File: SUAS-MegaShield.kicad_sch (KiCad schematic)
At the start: 1 part

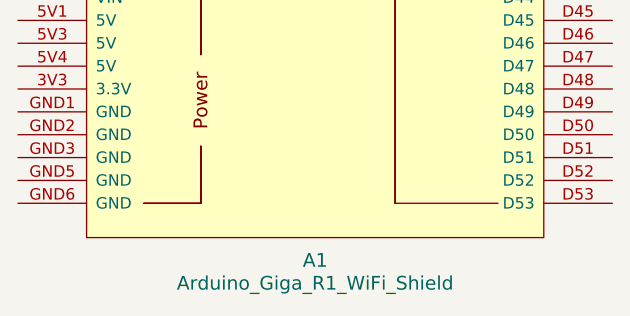
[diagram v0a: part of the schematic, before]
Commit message: Format Changes
- moved Silkscreen from front to back
- added edgeCut
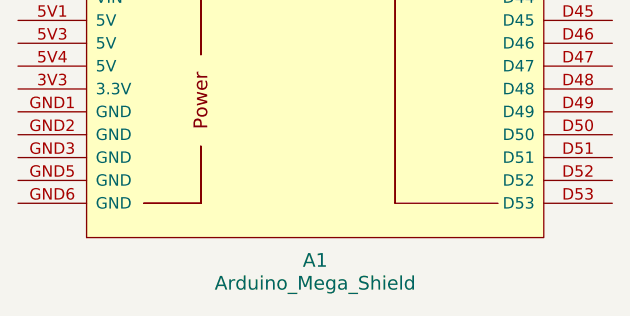
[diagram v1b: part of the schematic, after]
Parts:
- A1: value Arduino_Giga_R1_WiFi_Shield -> Arduino_Mega_Shield
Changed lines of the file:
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@@
 			)
 		)
-		(property "Value" "Arduino_Giga_R1_WiFi_Shield"
+		(property "Value" "Arduino_Mega_Shield"
 			(at 92.71 176.53 0)
 			(effects

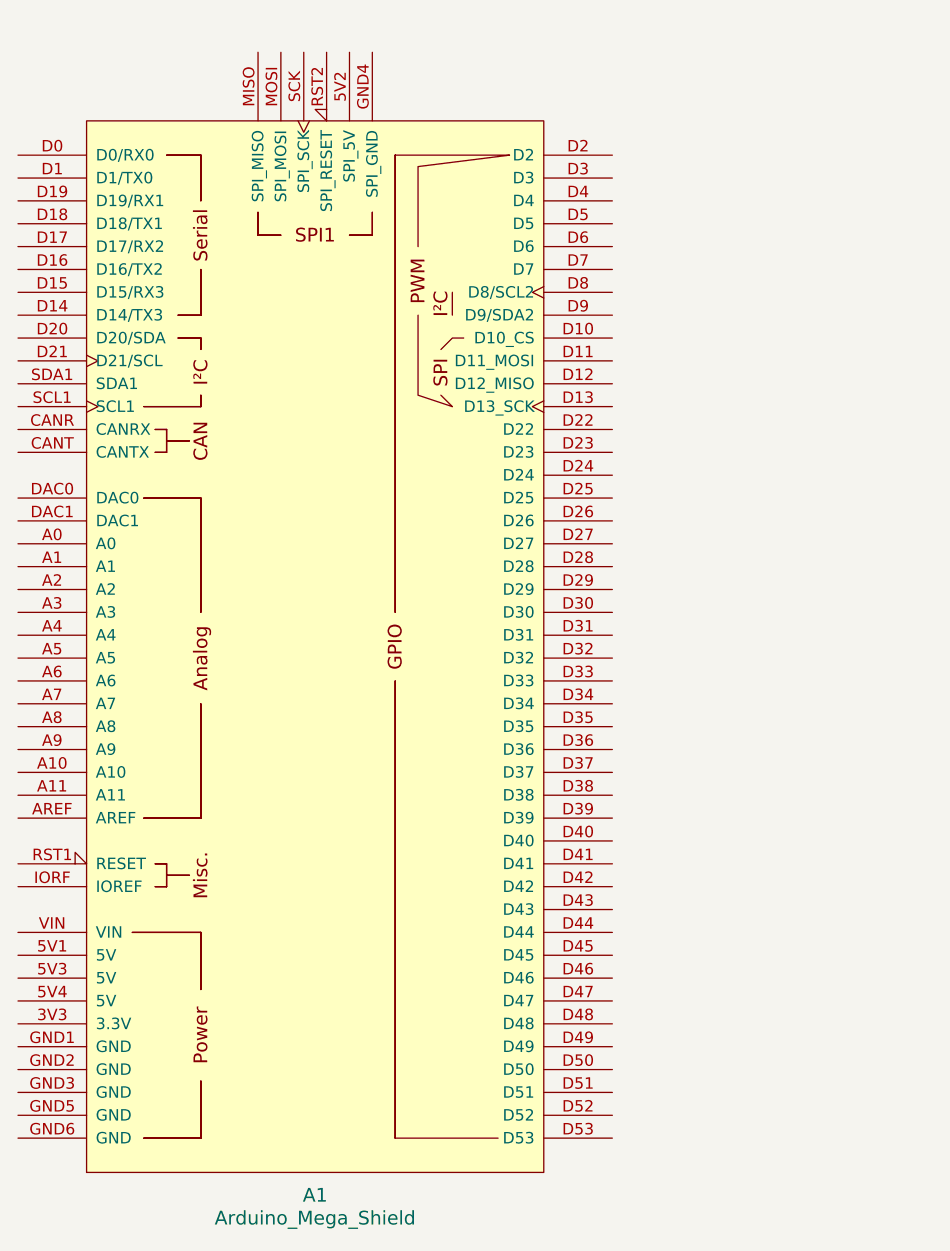
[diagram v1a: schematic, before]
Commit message: Vcc trace width adjustment
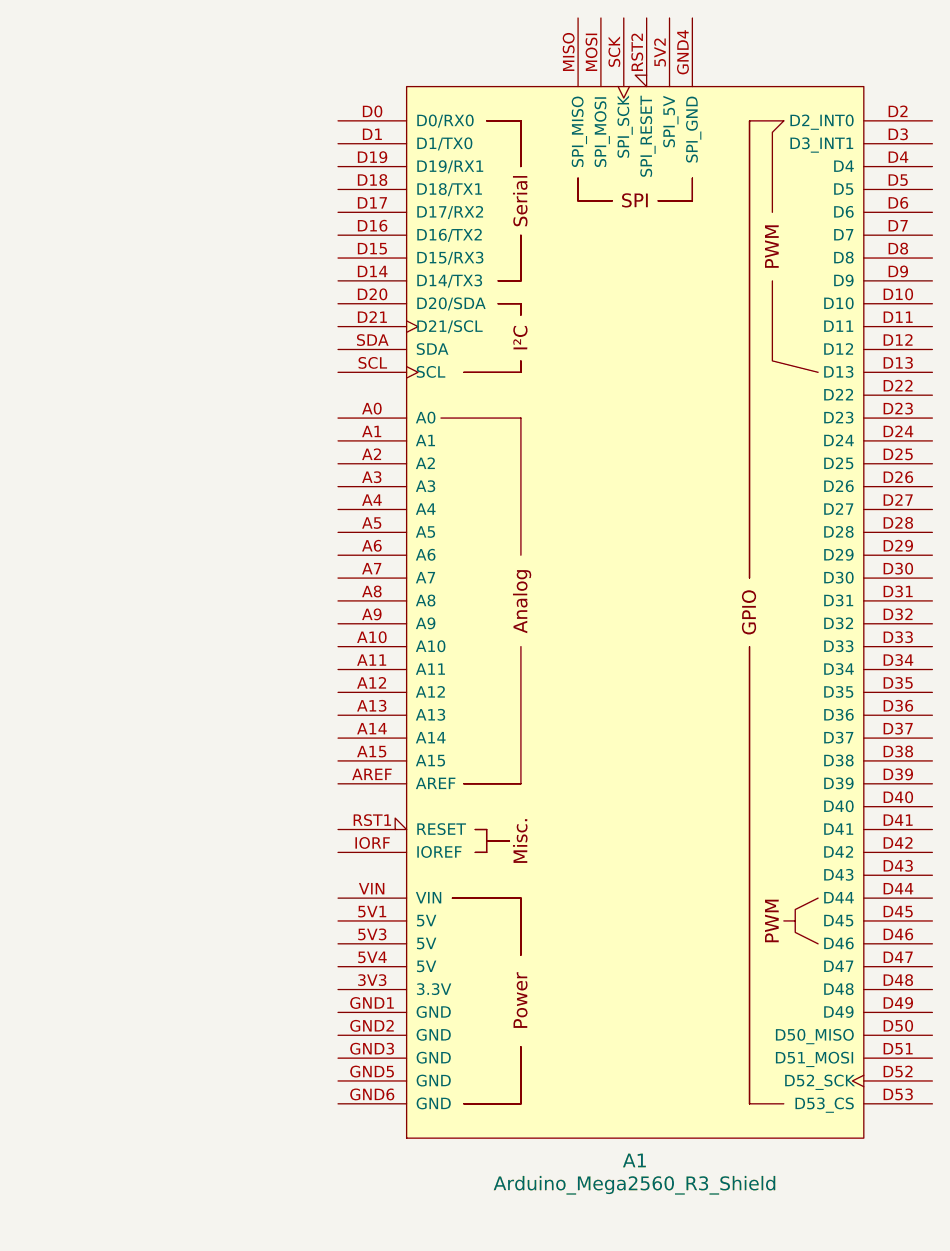
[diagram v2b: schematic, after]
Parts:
- removed A1: Arduino_Mega_Shield, arduino-library:Arduino_Giga_R1_WiFi_Shield, symbol arduino-library:Arduino_Giga_R1_WiFi_Shield
- added A1: Arduino_Mega2560_R3_Shield, arduino-library:Arduino_Mega2560_R3_Shield, symbol arduino-library:Arduino_Mega2560_R3_Shield
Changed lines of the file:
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@@
 	(paper "A4")
 	(symbol
-		(lib_id "arduino-library:Arduino_Giga_R1_WiFi_Shield")
-		(at 92.71 113.03 0)
+		(lib_id "arduino-library:Arduino_Mega2560_R3_Shield")
+		(at 128.27 109.22 0)
 		(unit 1)
 		(exclude_from_sim no)
@@
 		(fields_autoplaced yes)
 		(property "Reference" "A1"
-			(at 92.71 173.99 0)
-			(effects
-				(font
-					(size 1.524 1.524)
-				)
-			)
-		)
-		(property "Value" "Arduino_Mega_Shield"
-			(at 92.71 176.53 0)
-			(effects
-				(font
-					(size 1.524 1.524)
-				)
-			)
-		)
-		(property "Footprint" "arduino-library:Arduino_Giga_R1_WiFi_Shield"
-			(at 92.71 186.69 0)
+			(at 128.27 170.18 0)
+			(effects
+				(font
+					(size 1.524 1.524)
+				)
+			)
+		)
+		(property "Value" "Arduino_Mega2560_R3_Shield"
+			(at 128.27 172.72 0)
+			(effects
+				(font
+					(size 1.524 1.524)
+				)
+			)
+		)
+		(property "Footprint" "arduino-library:Arduino_Mega2560_R3_Shield"
+			(at 128.27 182.88 0)
 			(effects
 				(font
@@
 			)
 		)
-		(property "Datasheet" "https://docs.arduino.cc/hardware/giga-r1-wifi"
-			(at 92.71 182.88 0)
+		(property "Datasheet" "https://docs.arduino.cc/hardware/mega-2560"
+			(at 128.27 179.07 0)
 			(effects
 				(font
@@
 			)
 		)
-		(property "Description" "Shield for Arduino Giga R1 WiFi"
-			(at 92.71 113.03 0)
+		(property "Description" "Shield for Arduino Mega 2560 R3"
+			(at 128.27 109.22 0)
 			(effects
 				(font
@@
 			)
 		)
+		(pin "D12"
+		)
+		(pin "D16"
+		)
+		(pin "D18"
+		)
+		(pin "A15"
+		)
+		(pin "D23"
+		)
+		(pin "D26"
+		)
+		(pin "D29"
+		)
+		(pin "D41"
+		)
+		(pin "D22"
+		)
+		(pin "A1"
+		)
+		(pin "D24"
+		)
+		(pin "D4"
+		)
+		(pin "D35"
+		)
+		(pin "D14"
+		)
+		(pin "A5"
+		)
+		(pin "D19"
+		)
+		(pin "D43"
+		)
+		(pin "D42"
+		)
+		(pin "A8"
+		)
+		(pin "D44"
+		)
+		(pin "3V3"
+		)
+		(pin "D1"
+		)
+		(pin "D13"
+		)
+		(pin "A4"
+		)
+		(pin "A6"
+		)
+		(pin "D21"
+		)
+		(pin "D15"
+		)
+		(pin "D20"
+		)
+		(pin "D3"
+		)
+		(pin "D31"
+		)
+		(pin "D34"
+		)
+		(pin "A11"
+		)
+		(pin "D32"
+		)
+		(pin "D33"
+		)
+		(pin "D39"
+		)
+		(pin "AREF"
+		)
+		(pin "A0"
+		)
+		(pin "D2"
+		)
+		(pin "D28"
+		)
+		(pin "5V2"
+		)
+		(pin "A10"
+		)
+		(pin "A2"
+		)
+		(pin "D25"
+		)
+		(pin "A9"
+		)
+		(pin "A14"
+		)
+		(pin "D0"
+		)
+		(pin "D10"
+		)
+		(pin "D27"
+		)
+		(pin "D30"
+		)
+		(pin "D17"
+		)
+		(pin "D36"
+		)
+		(pin "D37"
+		)
 		(pin "D38"
 		)
-		(pin "D39"
-		)
-		(pin "D4"
+		(pin "5V4"
+		)
+		(pin "A12"
+		)
+		(pin "A7"
+		)
+		(pin "D11"
+		)
+		(pin "5V3"
 		)
 		(pin "D40"
 		)
-		(pin "D41"
-		)
-		(pin "D25"
-		)
-		(pin "D42"
-		)
-		(pin "D43"
-		)
-		(pin "D44"
+		(pin "5V1"
+		)
+		(pin "A13"
+		)
+		(pin "A3"
+		)
+		(pin "D50"
+		)
+		(pin "SCK"
+		)
+		(pin "D47"
+		)
+		(pin "GND3"
+		)
+		(pin "GND6"
+		)
+		(pin "D49"
+		)
+		(pin "D46"
+		)
+		(pin "GND4"
+		)
+		(pin "D48"
+		)
+		(pin "MISO"
+		)
+		(pin "RST1"
+		)
+		(pin "GND5"
+		)
+		(pin "SCL"
+		)
+		(pin "VIN"
+		)
+		(pin "SDA"
+		)
+		(pin "D7"
+		)
+		(pin "D52"
+		)
+		(pin "RST2"
+		)
+		(pin "IORF"
+		)
+		(pin "D6"
 		)
 		(pin "D45"
 		)
-		(pin "A4"
-		)
-		(pin "D24"
-		)
-		(pin "D46"
-		)
-		(pin "D47"
-		)
-		(pin "A3"
-		)
-		(pin "A1"
-		)
-		(pin "A7"
-		)
-		(pin "CANR"
-		)
-		(pin "D0"
-		)
-		(pin "D12"
-		)
-		(pin "D13"
-		)
-		(pin "D10"
-		)
-		(pin "D14"
-		)
-		(pin "D27"
-		)
-		(pin "D30"
-		)
-		(pin "A6"
-		)
-		(pin "D32"
-		)
-		(pin "A8"
-		)
-		(pin "AREF"
-		)
-		(pin "A5"
-		)
-		(pin "D15"
-		)
-		(pin "D17"
-		)
-		(pin "D11"
-		)
-		(pin "5V1"
-		)
-		(pin "D2"
-		)
-		(pin "D29"
-		)
-		(pin "5V3"
-		)
-		(pin "A0"
-		)
-		(pin "D31"
-		)
-		(pin "D33"
-		)
-		(pin "3V3"
-		)
-		(pin "D1"
-		)
-		(pin "D16"
-		)
-		(pin "5V2"
-		)
-		(pin "5V4"
-		)
-		(pin "A10"
-		)
-		(pin "D20"
-		)
-		(pin "A2"
-		)
-		(pin "D34"
-		)
-		(pin "D23"
-		)
-		(pin "D35"
-		)
-		(pin "CANT"
-		)
-		(pin "D36"
-		)
-		(pin "D21"
-		)
-		(pin "D3"
-		)
-		(pin "D37"
-		)
-		(pin "D18"
-		)
-		(pin "A11"
-		)
-		(pin "A9"
-		)
-		(pin "D19"
-		)
-		(pin "D28"
-		)
-		(pin "D22"
-		)
-		(pin "D26"
-		)
-		(pin "D50"
-		)
-		(pin "D52"
+		(pin "D53"
+		)
+		(pin "GND2"
+		)
+		(pin "D8"
 		)
 		(pin "D51"
 		)
-		(pin "DAC0"
-		)
-		(pin "GND3"
+		(pin "D5"
+		)
+		(pin "D9"
 		)
 		(pin "GND1"
 		)
-		(pin "SCL1"
-		)
-		(pin "D53"
-		)
-		(pin "MISO"
-		)
-		(pin "D5"
-		)
-		(pin "RST2"
-		)
-		(pin "GND6"
-		)
-		(pin "IORF"
-		)
-		(pin "D7"
-		)
-		(pin "GND5"
-		)
-		(pin "SCK"
-		)
-		(pin "D48"
-		)
-		(pin "VIN"
-		)
-		(pin "DAC1"
-		)
-		(pin "D49"
-		)
-		(pin "D8"
-		)
-		(pin "D9"
-		)
-		(pin "GND2"
-		)
-		(pin "D6"
-		)
 		(pin "MOSI"
 		)
-		(pin "GND4"
-		)
-		(pin "SDA1"
-		)
-		(pin "RST1"
-		)
 		(instances
-			(project ""
+			(project "SUAS-MegaShield"
 				(path "/e7bdfd97-9194-412d-a3f6-b05bc9b41b52"
 					(reference "A1")
